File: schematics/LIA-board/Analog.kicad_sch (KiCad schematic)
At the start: 0 parts

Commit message: some monor circuit changes
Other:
- added sheet oscillator (oscillator.kicad_sch)
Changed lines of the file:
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@@
 	(generator_version "10.0")
 	(paper "A4")
+	(sheet
+		(at 25.4 25.4)
+		(size 62.23 41.91)
+		(exclude_from_sim no)
+		(in_bom yes)
+		(on_board yes)
+		(dnp no)
+		(fields_autoplaced yes)
+		(stroke
+			(width 0.1524)
+			(type solid)
+		)
+		(fill
+			(color 0 0 0 0)
+		)
+		(property "Sheetname" "oscillator"
+			(at 25.4 24.6884 0)
+			(show_name no)
+			(do_not_autoplace no)
+			(effects
+				(font
+					(size 1.27 1.27)
+				)
+				(justify left bottom)
+			)
+		)
+		(property "Sheetfile" "oscillator.kicad_sch"
+			(at 25.4 67.8946 0)
+			(show_name no)
+			(do_not_autoplace no)
+			(effects
+				(font
+					(size 1.27 1.27)
+				)
+				(justify left top)
+			)
+		)
+		(instances
+			(project "GMOS-LIA"
+				(path "/87b3d1ed-39bd-4cff-a405-e580c48ff0ef/057bc398-9cad-4fbf-82b0-6414e0e9ecb2"
+					(page "4")
+				)
+			)
+		)
+	)
 )

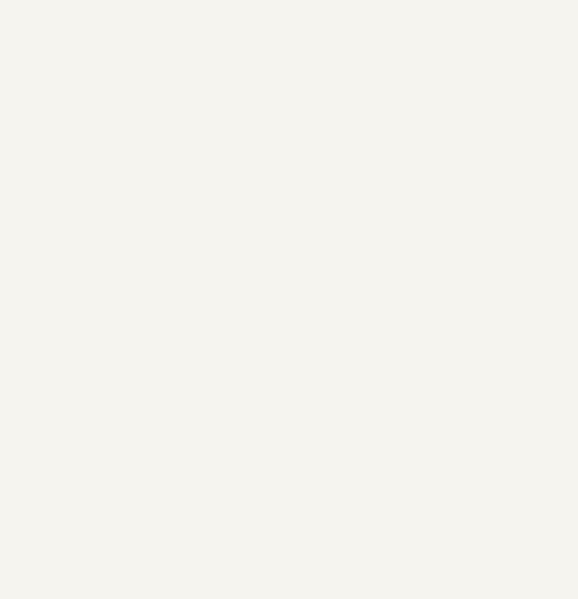
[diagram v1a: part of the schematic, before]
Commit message: some simulations, new page in kicad scematic
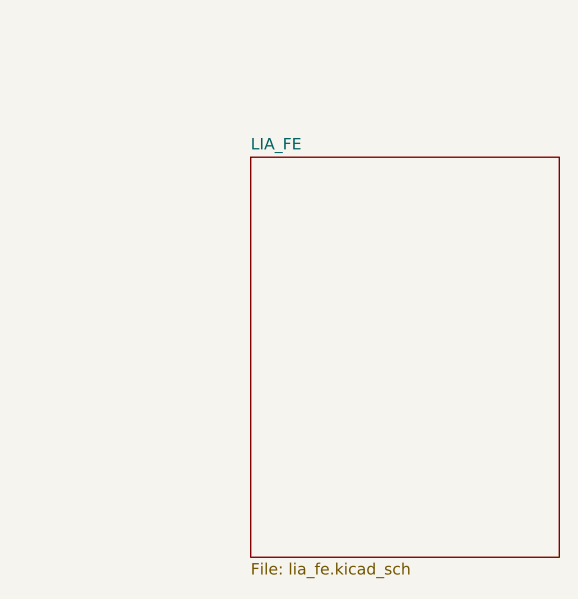
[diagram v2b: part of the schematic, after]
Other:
- added sheet LIA_FE (lia_fe.kicad_sch)
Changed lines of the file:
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@@
 	(paper "A4")
+	(sheet
+		(at 227.33 38.1)
+		(size 34.29 44.45)
+		(exclude_from_sim no)
+		(in_bom yes)
+		(on_board yes)
+		(dnp no)
+		(fields_autoplaced yes)
+		(stroke
+			(width 0.1524)
+			(type solid)
+		)
+		(fill
+			(color 0 0 0 0)
+		)
+		(property "Sheetname" "LIA_FE"
+			(at 227.33 37.3884 0)
+			(show_name no)
+			(do_not_autoplace no)
+			(effects
+				(font
+					(size 1.27 1.27)
+				)
+				(justify left bottom)
+			)
+		)
+		(property "Sheetfile" "lia_fe.kicad_sch"
+			(at 227.33 83.1346 0)
+			(show_name no)
+			(do_not_autoplace no)
+			(effects
+				(font
+					(size 1.27 1.27)
+				)
+				(justify left top)
+			)
+		)
+		(instances
+			(project "GMOS-LIA"
+				(path "/87b3d1ed-39bd-4cff-a405-e580c48ff0ef/057bc398-9cad-4fbf-82b0-6414e0e9ecb2"
+					(page "6")
+				)
+			)
+		)
+	)
 	(sheet
 		(at 25.4 25.4)

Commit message: all current changes
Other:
- sheet LIA_FE ports: added X_readout, X_sync, Y_readout, Y_sync, active_readout, blind_readout, cos, sin; removed none
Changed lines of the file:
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@@
 	(paper "A4")
 	(sheet
-		(at 227.33 38.1)
+		(at 170.815 78.105)
 		(size 34.29 44.45)
 		(exclude_from_sim no)
@@
 		)
 		(property "Sheetname" "LIA_FE"
-			(at 227.33 37.3884 0)
+			(at 170.815 77.3934 0)
 			(show_name no)
 			(do_not_autoplace no)
@@
 		)
 		(property "Sheetfile" "lia_fe.kicad_sch"
-			(at 227.33 83.1346 0)
+			(at 170.815 123.1396 0)
 			(show_name no)
 			(do_not_autoplace no)
@@
 				)
 				(justify left top)
+			)
+		)
+		(pin "active_readout" input
+			(at 170.815 85.09 180)
+			(effects
+				(font
+					(size 1.27 1.27)
+				)
+				(justify left)
+			)
+		)
+		(pin "blind_readout" input
+			(at 170.815 90.17 180)
+			(effects
+				(font
+					(size 1.27 1.27)
+				)
+				(justify left)
+			)
+		)
+		(pin "cos" input
+			(at 170.815 95.25 180)
+			(effects
+				(font
+					(size 1.27 1.27)
+				)
+				(justify left)
+			)
+		)
+		(pin "sin" input
+			(at 170.815 111.76 180)
+			(effects
+				(font
+					(size 1.27 1.27)
+				)
+				(justify left)
+			)
+		)
+		(pin "X_readout" output
+			(at 205.105 85.09 0)
+			(effects
+				(font
+					(size 1.27 1.27)
+				)
+				(justify right)
+			)
+		)
+		(pin "X_sync" output
+			(at 205.105 90.17 0)
+			(effects
+				(font
+					(size 1.27 1.27)
+				)
+				(justify right)
+			)
+		)
+		(pin "Y_readout" output
+			(at 205.105 95.25 0)
+			(effects
+				(font
+					(size 1.27 1.27)
+				)
+				(justify right)
+			)
+		)
+		(pin "Y_sync" output
+			(at 205.105 100.33 0)
+			(effects
+				(font
+					(size 1.27 1.27)
+				)
+				(justify right)
 			)
 		)
@@
 	)
 	(sheet
-		(at 25.4 25.4)
+		(at 55.88 82.55)
 		(size 62.23 41.91)
 		(exclude_from_sim no)
@@
 		)
 		(property "Sheetname" "oscillator"
-			(at 25.4 24.6884 0)
+			(at 55.88 81.8384 0)
 			(show_name no)
 			(do_not_autoplace no)
@@
 		)
 		(property "Sheetfile" "oscillator.kicad_sch"
-			(at 25.4 67.8946 0)
+			(at 55.88 125.0446 0)
 			(show_name no)
 			(do_not_autoplace no)

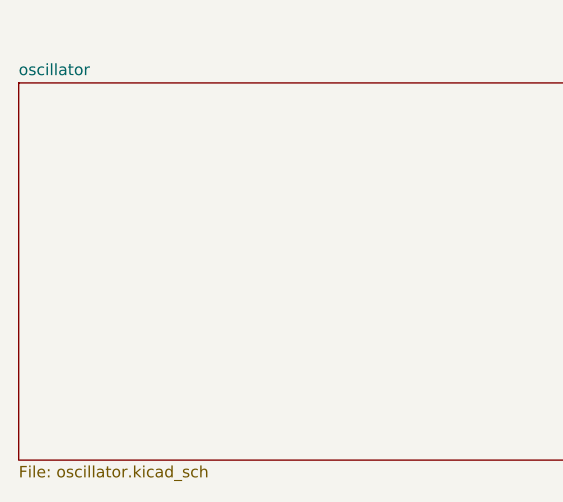
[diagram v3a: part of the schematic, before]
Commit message: new oscillator, not tested in simulation yet
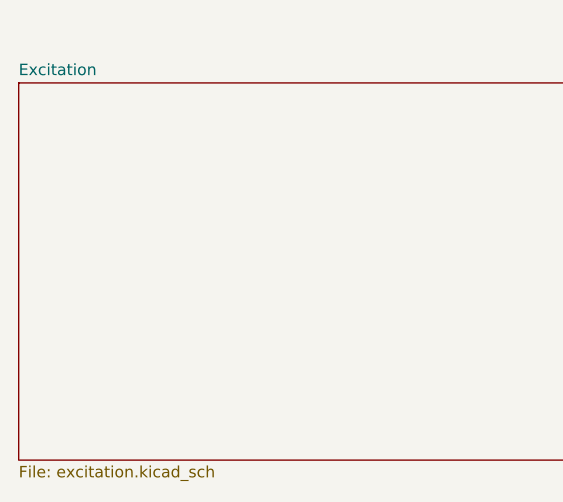
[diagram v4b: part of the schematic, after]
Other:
- sheet oscillator renamed Excitation
- sheet Excitation: file oscillator.kicad_sch -> excitation.kicad_sch
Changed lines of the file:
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@@
 			(color 0 0 0 0)
 		)
-		(property "Sheetname" "oscillator"
+		(property "Sheetname" "Excitation"
 			(at 55.88 81.8384 0)
 			(show_name no)
@@
 			)
 		)
-		(property "Sheetfile" "oscillator.kicad_sch"
+		(property "Sheetfile" "excitation.kicad_sch"
 			(at 55.88 125.0446 0)
 			(show_name no)

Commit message: commit before changing LIA
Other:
- added sheet GMOS_soc (gmos_mux2.kicad_sch)
- sheet Excitation ports: added Exct[0..1], ext0_vadj, ext1_vadj, mcu_sin; removed none
- sheet LIA_FE ports: added X_chop, Y_chop; removed cos, sin
